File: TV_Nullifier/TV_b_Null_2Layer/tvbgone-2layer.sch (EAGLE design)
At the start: 18 parts, among them IC1 ATTINY85V-10S, Q1 BC857AT115, Q2 PMBT3904VS_DUAL_NPN, Y1_8MHZ RESONATOR

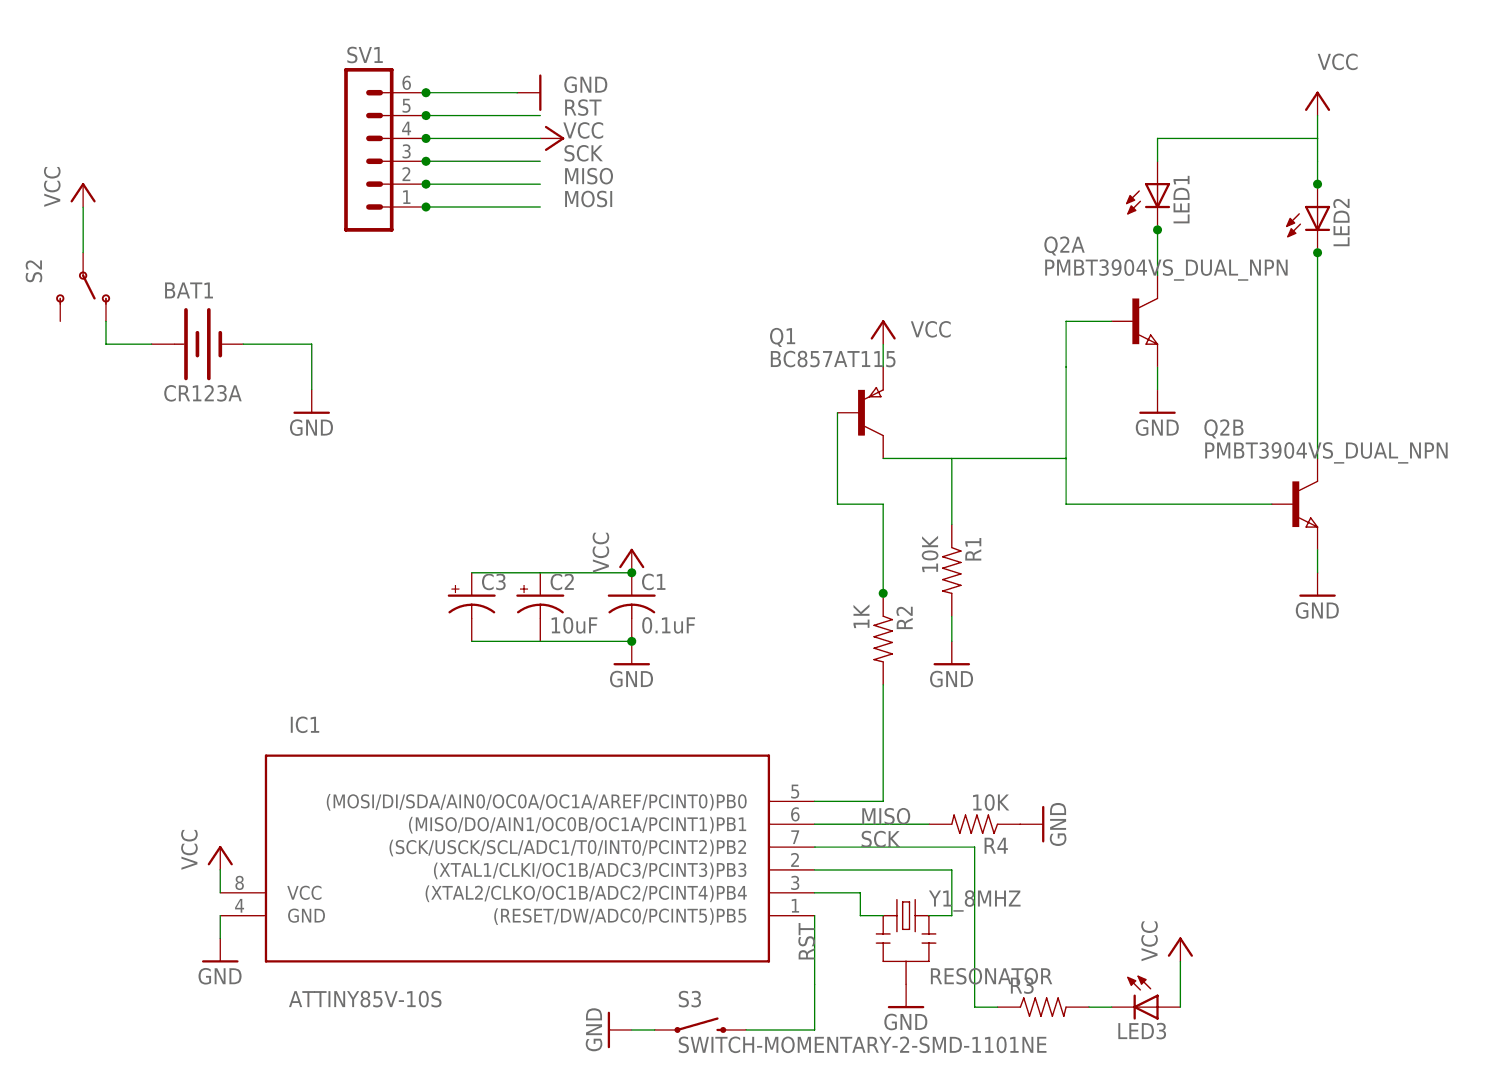
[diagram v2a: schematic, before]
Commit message: 
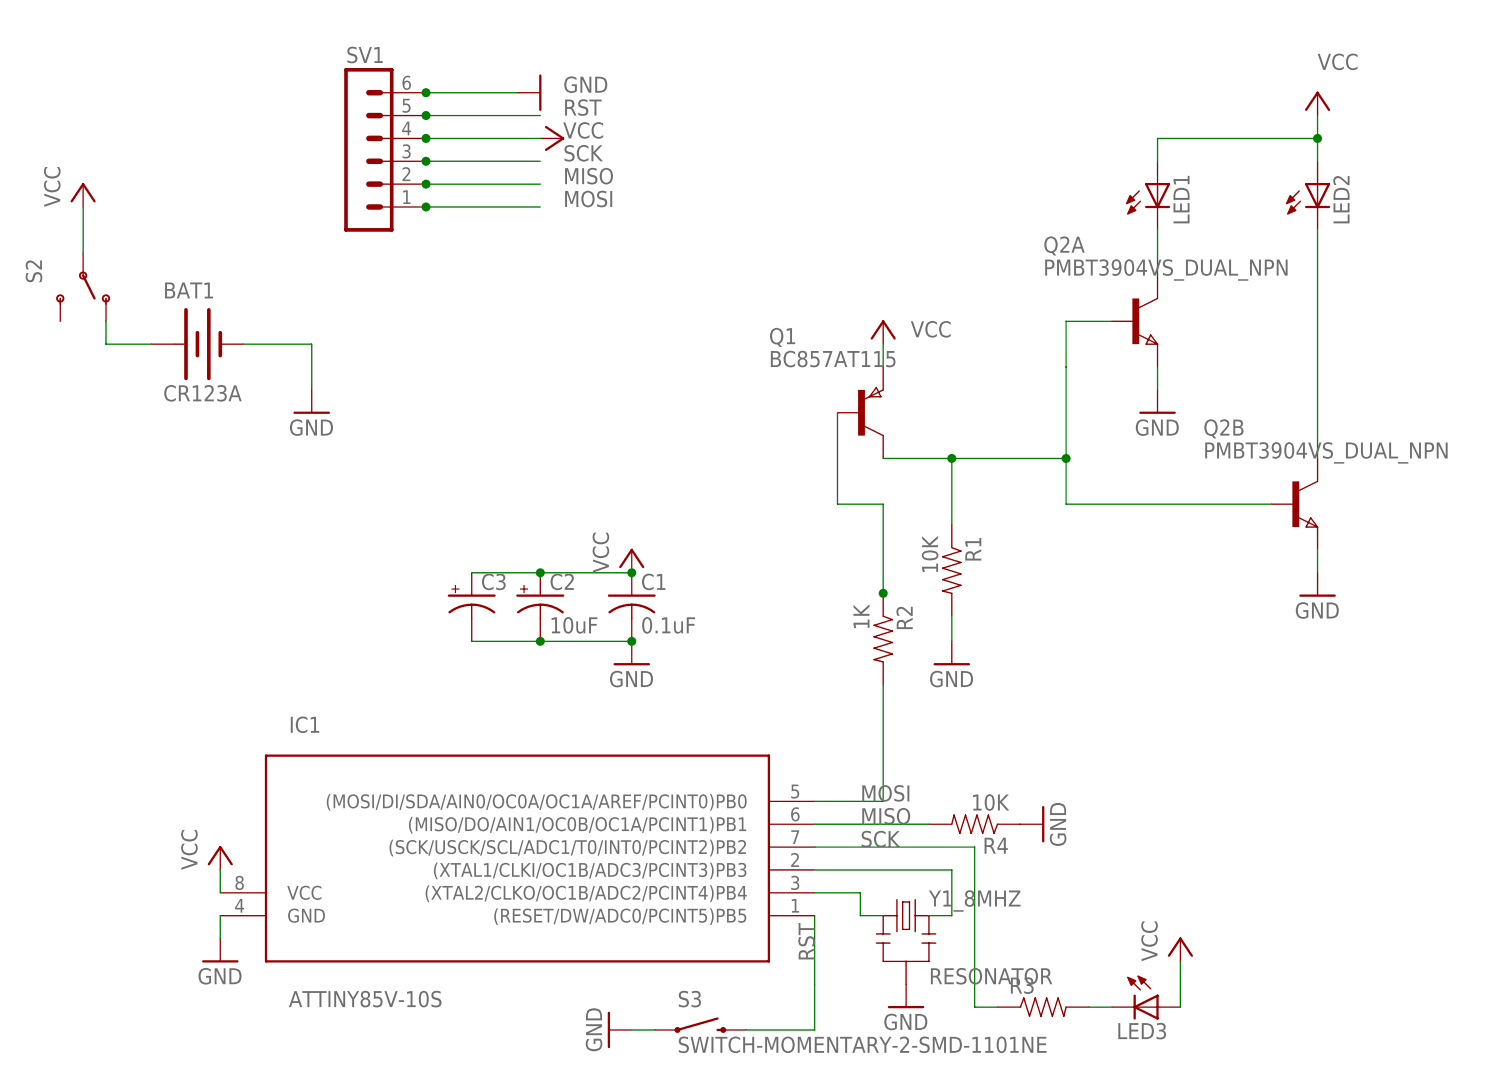
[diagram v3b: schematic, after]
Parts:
- LED1, LED2: device tvbgone3:LEDSIDEIR -> tvbgone-2layer:TVBGONE3_LEDSIDEIR
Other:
- moved on the sheet: LED2
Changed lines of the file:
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@@
 <?xml version="1.0" encoding="utf-8"?>
 <!DOCTYPE eagle SYSTEM "eagle.dtd">
-<eagle version="6.4">
+<eagle version="6.5.0">
 <drawing>
 <settings>
@@
 <part name="Q1" library="zetex" deviceset="PNPSOT323" device="SOT416" value="BC857AT115"/>
 <part name="P+7" library="supply1" deviceset="VCC" device=""/>
-<part name="LED1" library="tvbgone3" deviceset="LED" device="SIDEIR"/>
-<part name="LED2" library="tvbgone3" deviceset="LED" device="SIDEIR"/>
+<part name="LED1" library="tvbgone-2layer" deviceset="TVBGONE3_LED" device="SIDEIR"/>
+<part name="LED2" library="tvbgone-2layer" deviceset="TVBGONE3_LED" device="SIDEIR"/>
 <part name="R2" library="SparkFun" deviceset="RESISTOR" device="" value="1K"/>
 <part name="S2" library="SparkFun-Electromechanical" deviceset="SWITCH-SPDT" device="-SMD-A"/>
@@
 <attribute name="VALUE" x="147.955" y="137.668" size="1.778" layer="96" rot="R90"/>
 </instance>
-<instance part="LED2" gate="G$1" x="160.02" y="139.7" smashed="yes">
-<attribute name="NAME" x="163.576" y="135.128" size="1.778" layer="95" rot="R90"/>
-<attribute name="VALUE" x="165.735" y="135.128" size="1.778" layer="96" rot="R90"/>
+<instance part="LED2" gate="G$1" x="160.02" y="142.24" smashed="yes">
+<attribute name="NAME" x="163.576" y="137.668" size="1.778" layer="95" rot="R90"/>
+<attribute name="VALUE" x="165.735" y="137.668" size="1.778" layer="96" rot="R90"/>
 </instance>
 <instance part="R2" gate="G$1" x="111.76" y="91.694" smashed="yes" rot="R270">
@@
 <pinref part="C3" gate="G$1" pin="+"/>
 <wire x1="73.66" y1="99.06" x2="66.04" y2="99.06" width="0.1524" layer="91"/>
+<junction x="73.66" y="99.06"/>
 </segment>
 <segment>
@@
 </segment>
 <segment>
-<wire x1="160.02" y1="142.24" x2="160.02" y2="144.78" width="0.1524" layer="91"/>
 <wire x1="160.02" y1="144.78" x2="160.02" y2="147.32" width="0.1524" layer="91"/>
-<junction x="160.02" y="142.24"/>
 <pinref part="P+3" gate="VCC" pin="VCC"/>
 <pinref part="LED2" gate="G$1" pin="A"/>
@@
 <wire x1="142.24" y1="144.78" x2="142.24" y2="147.32" width="0.1524" layer="91"/>
 <wire x1="142.24" y1="147.32" x2="160.02" y2="147.32" width="0.1524" layer="91"/>
+<junction x="160.02" y="147.32"/>
 </segment>
 <segment>
@@
 <pinref part="C3" gate="G$1" pin="-"/>
 <wire x1="66.04" y1="91.44" x2="73.66" y2="91.44" width="0.1524" layer="91"/>
+<junction x="73.66" y="91.44"/>
 </segment>
 <segment>
@@
 <pinref part="IC1" gate="G$1" pin="(MOSI/DI/SDA/AIN0/OC0A/OC1A/AREF/PCINT0)PB0"/>
 <pinref part="R2" gate="G$1" pin="2"/>
+<label x="109.22" y="73.66" size="1.778" layer="95"/>
 </segment>
 </net>
@@
 <segment>
 <wire x1="142.24" y1="137.16" x2="142.24" y2="132.08" width="0.1524" layer="91"/>
-<junction x="142.24" y="137.16"/>
 <pinref part="LED1" gate="G$1" pin="C"/>
 <pinref part="Q2" gate="A" pin="C"/>
@@
 <net name="N$5" class="0">
 <segment>
-<wire x1="160.02" y1="134.62" x2="160.02" y2="111.76" width="0.1524" layer="91"/>
-<junction x="160.02" y="134.62"/>
+<wire x1="160.02" y1="137.16" x2="160.02" y2="111.76" width="0.1524" layer="91"/>
 <pinref part="LED2" gate="G$1" pin="C"/>
 <pinref part="Q2" gate="B" pin="C"/>
@@
 <pinref part="Q2" gate="B" pin="B"/>
 <wire x1="132.08" y1="111.76" x2="132.08" y2="106.68" width="0.1524" layer="91"/>
-</segment>
-</net>
+<junction x="119.38" y="111.76"/>
+<junction x="132.08" y="111.76"/>
+</segment>
+</net>

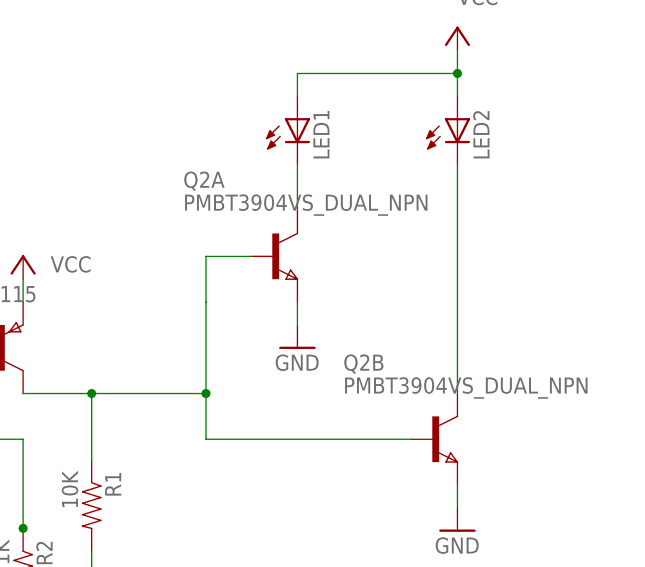
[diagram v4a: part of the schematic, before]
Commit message: 
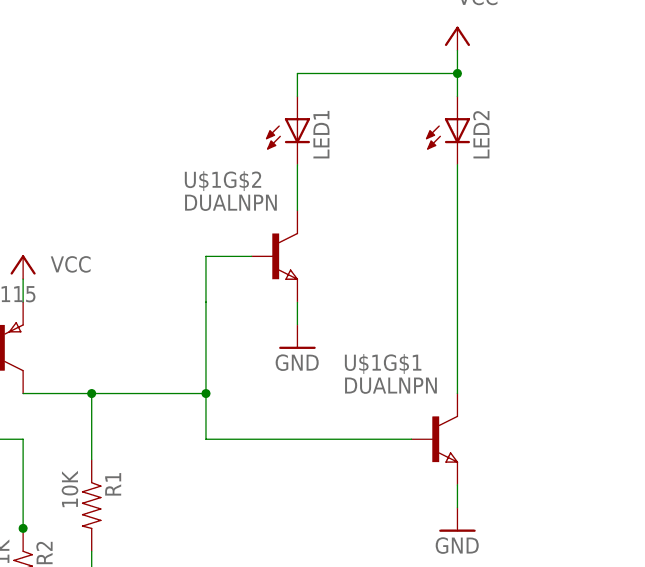
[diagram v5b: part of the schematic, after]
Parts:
- removed Q2: PMBT3904VS_DUAL_NPN, tvbgone-2layer:PMBT3904VS_DUAL_NPN
- added U$1: DUALNPN, 6x6:DUALNPN
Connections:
- net GND: now also U$1G$1.E, U$1G$2.E; no longer Q2A.E, Q2B.E
- net N$4: now also U$1G$2.C; no longer Q2A.C
- net N$5: now also U$1G$1.C; no longer Q2B.C
- net N$9: now also U$1G$1.B, U$1G$2.B; no longer Q2A.B, Q2B.B

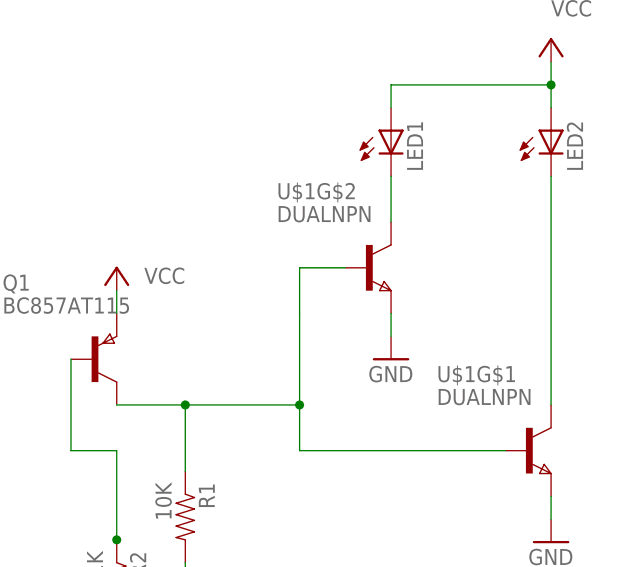
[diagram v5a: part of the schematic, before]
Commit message: 
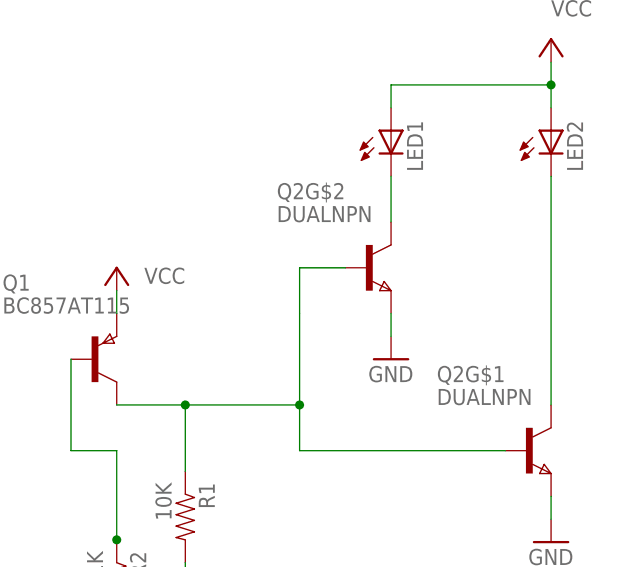
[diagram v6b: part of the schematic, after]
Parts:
- renumbered U$1 to Q2
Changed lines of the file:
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@@
 <part name="S3" library="SparkFun-Electromechanical" deviceset="SWITCH-MOMENTARY-2" device="-SMD-1101NE"/>
 <part name="C3" library="tvbgone-2layer" deviceset="SPARKFUN_CAP_POL" device="3528"/>
-<part name="U$1" library="6x6" deviceset="DUALNPN" device=""/>
+<part name="Q2" library="6x6" deviceset="DUALNPN" device=""/>
 </parts>
 <sheets>
@@
 <instance part="S3" gate="G$1" x="91.44" y="48.26"/>
 <instance part="C3" gate="G$1" x="66.04" y="96.52"/>
-<instance part="U$1" gate="G$1" x="157.48" y="106.68"/>
-<instance part="U$1" gate="G$2" x="139.7" y="127"/>
+<instance part="Q2" gate="G$1" x="157.48" y="106.68"/>
+<instance part="Q2" gate="G$2" x="139.7" y="127"/>
 </instances>
 <busses>
@@
 <wire x1="160.02" y1="101.6" x2="160.02" y2="99.06" width="0.1524" layer="91"/>
 <pinref part="GND9" gate="1" pin="GND"/>
-<pinref part="U$1" gate="G$1" pin="E"/>
+<pinref part="Q2" gate="G$1" pin="E"/>
 </segment>
 <segment>
 <wire x1="142.24" y1="121.92" x2="142.24" y2="119.38" width="0.1524" layer="91"/>
 <pinref part="GND12" gate="1" pin="GND"/>
-<pinref part="U$1" gate="G$2" pin="E"/>
+<pinref part="Q2" gate="G$2" pin="E"/>
 </segment>
 <segment>
@@
 <wire x1="142.24" y1="137.16" x2="142.24" y2="132.08" width="0.1524" layer="91"/>
 <pinref part="LED1" gate="G$1" pin="C"/>
-<pinref part="U$1" gate="G$2" pin="C"/>
+<pinref part="Q2" gate="G$2" pin="C"/>
 </segment>
 </net>
@@
 <wire x1="160.02" y1="137.16" x2="160.02" y2="111.76" width="0.1524" layer="91"/>
 <pinref part="LED2" gate="G$1" pin="C"/>
-<pinref part="U$1" gate="G$1" pin="C"/>
+<pinref part="Q2" gate="G$1" pin="C"/>
 </segment>
 </net>
@@
 <junction x="119.38" y="111.76"/>
 <junction x="132.08" y="111.76"/>
-<pinref part="U$1" gate="G$1" pin="B"/>
-<pinref part="U$1" gate="G$2" pin="B"/>
-</segment>
-</net>
+<pinref part="Q2" gate="G$1" pin="B"/>
+<pinref part="Q2" gate="G$2" pin="B"/>
+</segment>
+</net>

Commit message: 
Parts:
- R3: value 1.5K -> 1K
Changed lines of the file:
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@@
 <part name="LED3" library="minimidi" deviceset="LED" device="CHIPLED_0603"/>
 <part name="P+6" library="supply1" deviceset="VCC" device=""/>
-<part name="R3" library="SparkFun" deviceset="RESISTOR" device="" value="1.5K"/>
+<part name="R3" library="SparkFun" deviceset="RESISTOR" device="" value="1K"/>
 <part name="GND9" library="supply1" deviceset="GND" device=""/>
 <part name="GND10" library="supply1" deviceset="GND" device=""/>
